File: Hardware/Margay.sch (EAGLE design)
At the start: 60 parts, among them IC1 ATMEGA644M, J1 CONN_4SCREW_2.54, J2 CONN_6, Q1 MOSFET_PCH-IRLML2244, Q2 MOSFET-NCH-DMG3404L, Q5 MOSFET_PCH-IRLML2244, U2 FT231X-Q

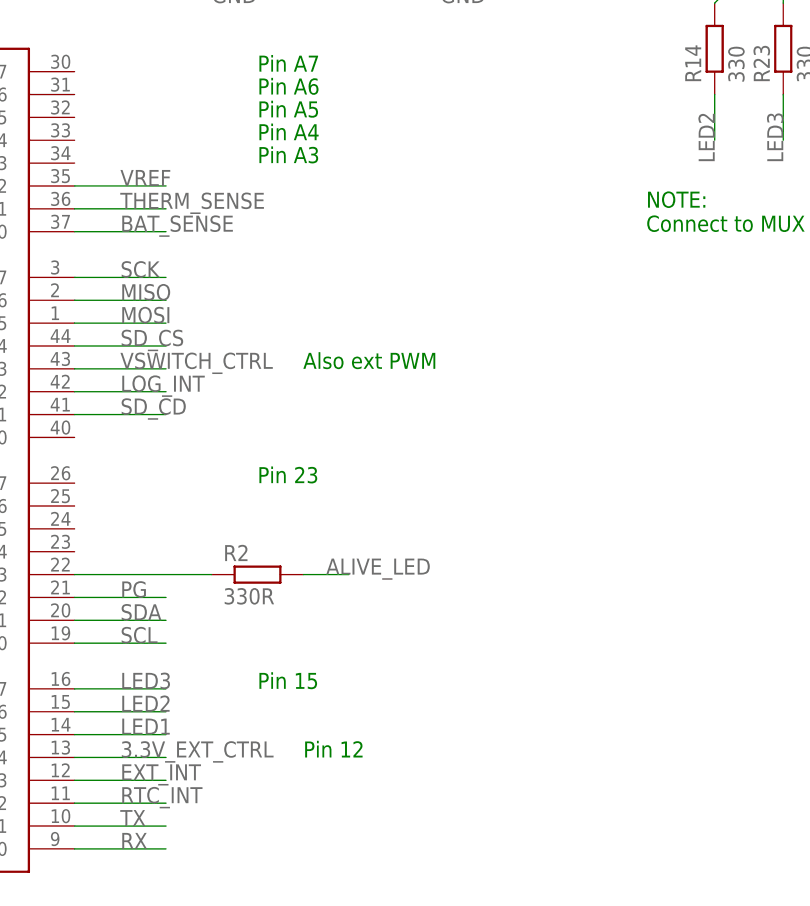
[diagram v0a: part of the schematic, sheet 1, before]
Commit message: Added software folder to repo
Software folder containing hardware test script as well as logger code which supports the TP-Downhole
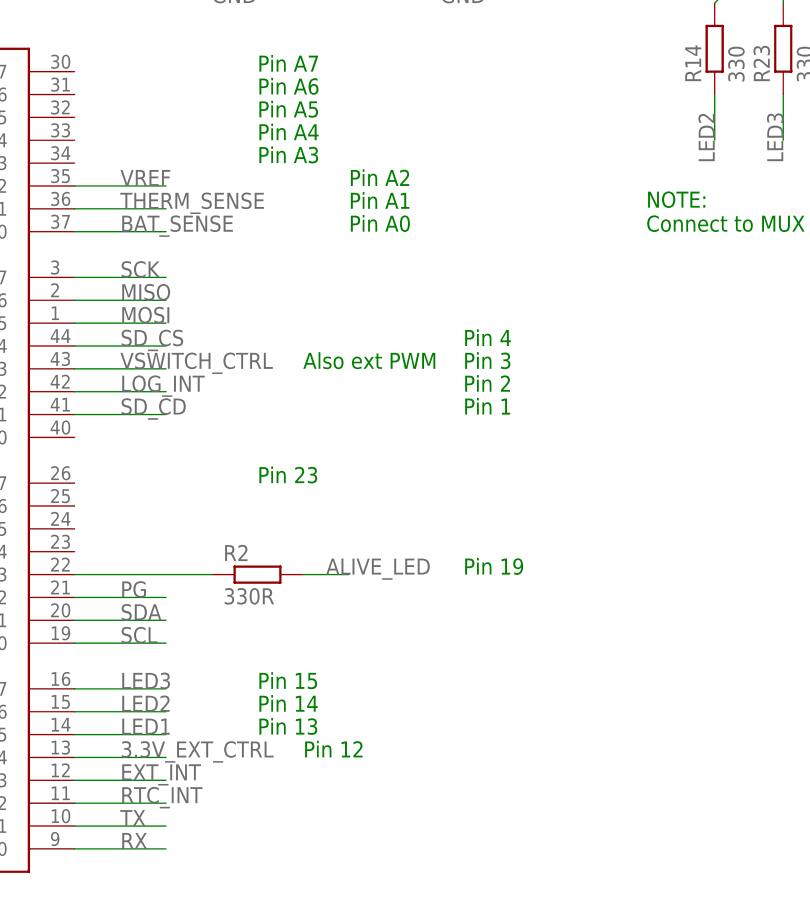
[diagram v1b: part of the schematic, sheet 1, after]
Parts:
- J2: value CONN_6 -> CONN_6SCREW_2.54; device bschulz:CONN_6 -> bschulz:CONN_6SCREW_2.54
- J3, J4, J5: device bschulz:CONN_022.54MM_SCREWTERM -> bschulz:CONN_02SCREW_2.54
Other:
- note added: "Pin 1"
- note added: "Pin 13"
- note added: "Pin 14"
- note added: "Pin 19"
- note added: "Pin 2"
- note added: "Pin 3"
- note added: "Pin 4"
- note added: "Pin A0"
- note added: "Pin A1"
- note added: "Pin A2"
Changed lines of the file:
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@@
 <layer number="18" name="Vias" color="2" fill="1" visible="no" active="no"/>
 <layer number="19" name="Unrouted" color="6" fill="1" visible="no" active="no"/>
-<layer number="20" name="Dimension" color="15" fill="1" visible="no" active="no"/>
+<layer number="20" name="Dimension" color="24" fill="1" visible="no" active="no"/>
 <layer number="21" name="tPlace" color="7" fill="1" visible="no" active="no"/>
 <layer number="22" name="bPlace" color="7" fill="1" visible="no" active="no"/>
@@
 <part name="GND32" library="supply1" library_urn="urn:adsk.eagle:library:371" deviceset="GND" device=""/>
 <part name="J1" library="bschulz" deviceset="CONN_4" device="SCREW_2.54"/>
-<part name="J2" library="bschulz" deviceset="CONN_6" device=""/>
-<part name="J3" library="bschulz" deviceset="CONN_02" device="2.54MM_SCREWTERM"/>
-<part name="J4" library="bschulz" deviceset="CONN_02" device="2.54MM_SCREWTERM"/>
-<part name="J5" library="bschulz" deviceset="CONN_02" device="2.54MM_SCREWTERM"/>
+<part name="J2" library="bschulz" deviceset="CONN_6" device="SCREW_2.54"/>
+<part name="J3" library="bschulz" deviceset="CONN_02" device="SCREW_2.54"/>
+<part name="J4" library="bschulz" deviceset="CONN_02" device="SCREW_2.54"/>
+<part name="J5" library="bschulz" deviceset="CONN_02" device="SCREW_2.54"/>
 <part name="R12" library="bschulz" deviceset="R-EU_" device="R0603" value="10k"/>
 <part name="JP2" library="SparkFun-Jumpers" library_urn="urn:adsk.eagle:library:528" deviceset="JUMPER-SMT_2_NC_PASTE" device="_SILK" package3d_urn="urn:adsk.eagle:package:39282/1"/>
@@
 <text x="327.66" y="231.14" size="1.778" layer="91">add voltage divider??</text>
 <text x="180.34" y="170.18" size="1.778" layer="91">Reverse Polarity Protection</text>
+<text x="175.26" y="55.88" size="1.778" layer="91">Pin 19</text>
+<text x="152.4" y="40.64" size="1.778" layer="91">Pin 14</text>
+<text x="152.4" y="38.1" size="1.778" layer="91">Pin 13</text>
+<text x="175.26" y="78.74" size="1.778" layer="91">Pin 3</text>
+<text x="175.26" y="76.2" size="1.778" layer="91">Pin 2</text>
+<text x="175.26" y="73.66" size="1.778" layer="91">Pin 1</text>
+<text x="175.26" y="81.28" size="1.778" layer="91">Pin 4</text>
+<text x="162.56" y="93.98" size="1.778" layer="91">Pin A0</text>
+<text x="162.56" y="96.52" size="1.778" layer="91">Pin A1</text>
+<text x="162.56" y="99.06" size="1.778" layer="91">Pin A2</text>
 </plain>
 <instances>

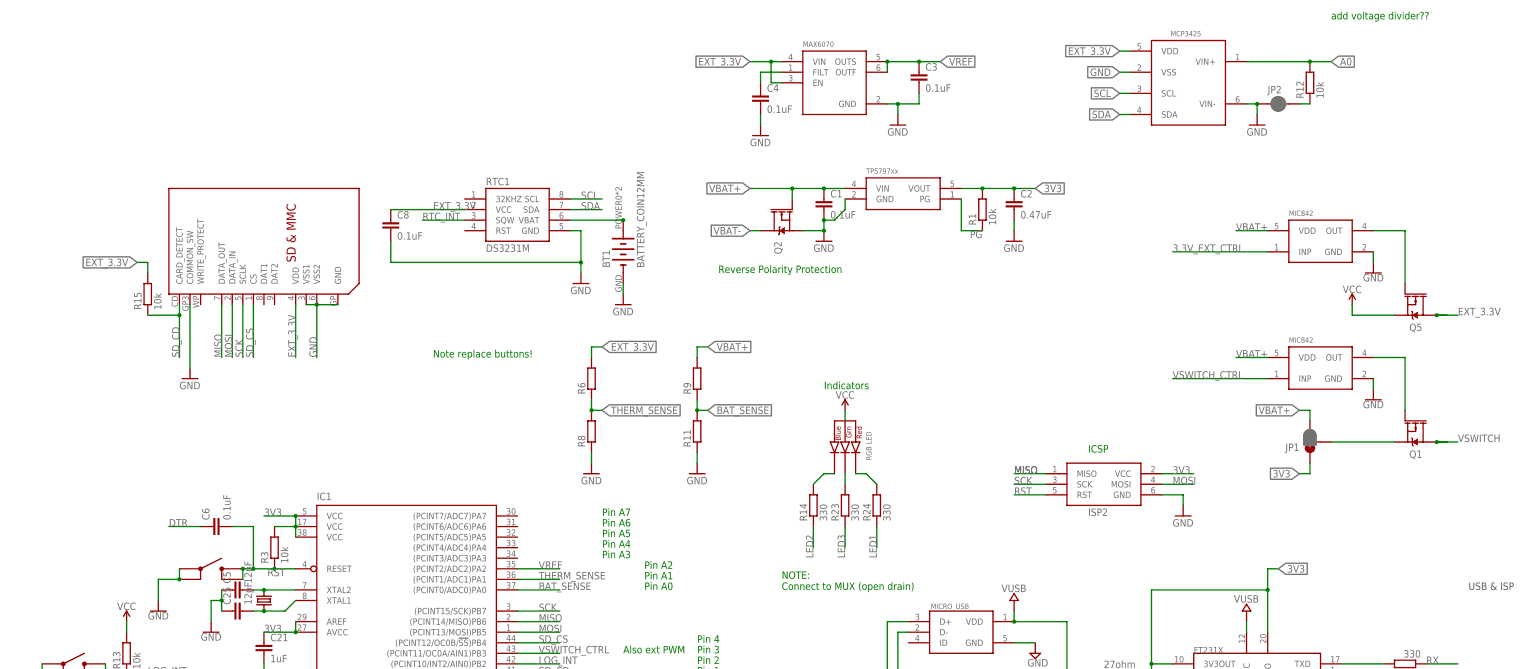
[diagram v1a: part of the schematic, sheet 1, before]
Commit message: Added revision notes to board
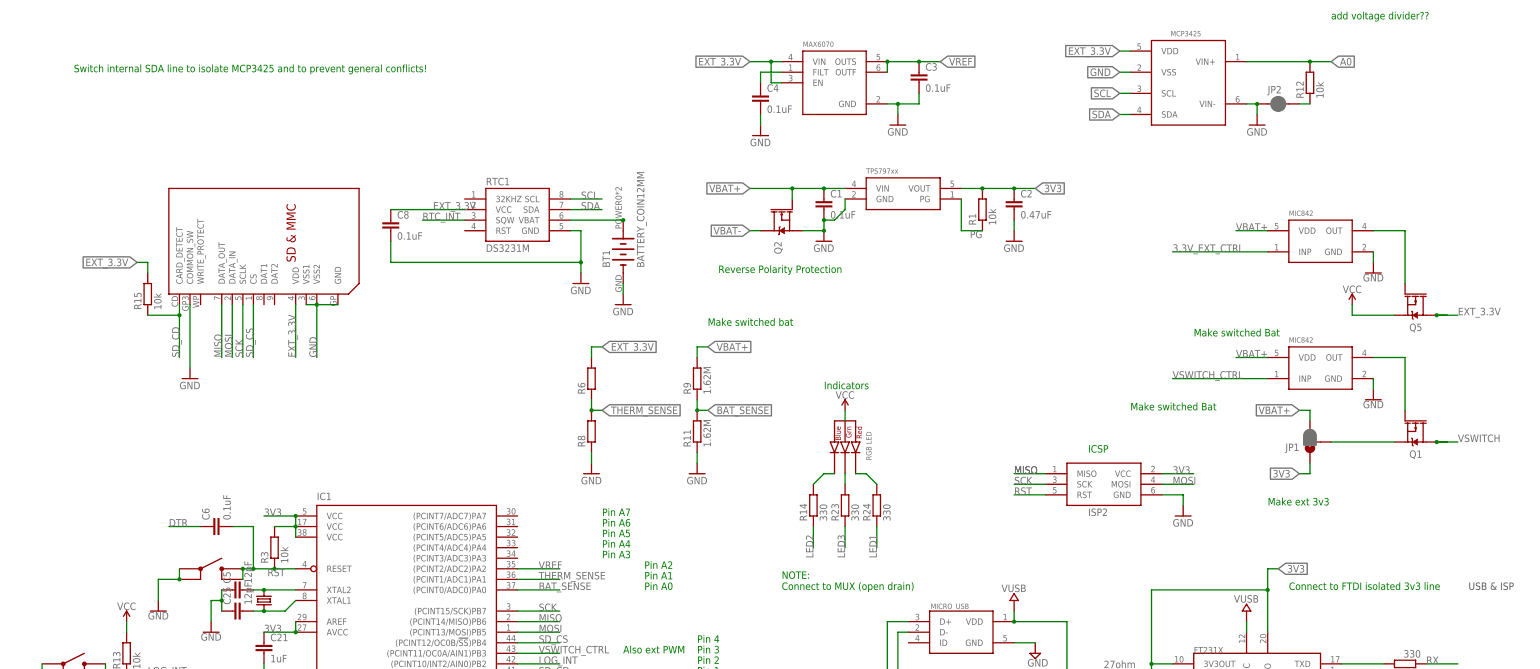
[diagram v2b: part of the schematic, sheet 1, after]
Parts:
- R11, R9: value (none) -> 1.62M
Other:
- note added: "Connect to FTDI isolated 3v3 line"
- note added: "Make ext 3v3"
- note added: "Make switched Bat"
- note added: "Make switched bat"
- note added: "Switch internal SDA line to isolate MCP3425 and to prevent general conflicts!"
- note removed: "Note replace buttons!"
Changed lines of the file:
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@@
 <part name="R6" library="bschulz" deviceset="R-EU_" device="R0603"/>
 <part name="R8" library="bschulz" deviceset="R-EU_" device="R0603"/>
-<part name="R9" library="bschulz" deviceset="R-EU_" device="R0603"/>
-<part name="R11" library="bschulz" deviceset="R-EU_" device="R0603"/>
+<part name="R9" library="bschulz" deviceset="R-EU_" device="R0603" value="1.62M"/>
+<part name="R11" library="bschulz" deviceset="R-EU_" device="R0603" value="1.62M"/>
 <part name="GND4" library="supply1" library_urn="urn:adsk.eagle:library:371" deviceset="GND" device=""/>
 <part name="GND5" library="supply1" library_urn="urn:adsk.eagle:library:371" deviceset="GND" device=""/>
@@
 <text x="195.58" y="93.98" size="1.778" layer="91">NOTE:
 Connect to MUX (open drain)</text>
-<text x="111.76" y="149.86" size="1.778" layer="91">Note replace buttons!</text>
 <text x="157.48" y="35.56" size="1.778" layer="91">Pin 12</text>
 <text x="152.4" y="111.76" size="1.778" layer="91">Pin A7</text>
@@
 <text x="162.56" y="96.52" size="1.778" layer="91">Pin A1</text>
 <text x="162.56" y="99.06" size="1.778" layer="91">Pin A2</text>
+<text x="312.42" y="114.3" size="1.778" layer="91">Make ext 3v3</text>
+<text x="279.4" y="137.16" size="1.778" layer="91">Make switched Bat</text>
+<text x="294.64" y="154.94" size="1.778" layer="91">Make switched Bat</text>
+<text x="177.8" y="157.48" size="1.778" layer="91">Make switched bat</text>
+<text x="25.4" y="218.44" size="1.778" layer="91">Switch internal SDA line to isolate MCP3425 and to prevent general conflicts!</text>
+<text x="317.5" y="93.98" size="1.778" layer="91">Connect to FTDI isolated 3v3 line</text>
 </plain>
 <instances>

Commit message: Margay 1.0 initial layout
Initial layout of the version 1.0 , solder jumpers currently not added, along with battery connector, may intoduce back later, needs cleanup and DRC
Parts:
- removed Q5: MOSFET_PCH-IRLML2244, bschulz:MOSFET_PCH-IRLML2244
- removed U$18: MIC842, bschulz:MIC842
- added C7: 0.1uF, bschulz_passives:C-EUC0603
- added C9: 0.47uF, bschulz_passives:C-EUC0603
- added Q3: 2N7002, bschulz:MOSFET-NCH-2N7002PW
- added Q4, Q6: FDN360P, bschulz:MOSFET_PCH-FDN360P
- added R16: 180k, bschulz_passives:R-EU_R0603
- added R17: 10k, bschulz_passives:R-EU_R0603
- added U$10: TPS79733, bschulz:TPS79733
- added U$11: MIC842H, bschulz:MIC842H
- added U$12, U$13: SN74LVC1G3157DRL, bschulz:SN74LVC1G3157DRL
- added U$17: SN74AUP3G34DCU, bschulz:SN74AUP3G34DCU
- D+, D-: device bschulz:R-EU_27R0603 -> bschulz_passives:R-EU_27R0603
- J1: value CONN_4SCREW_2.54 -> CONN_42.54_SCREW; device bschulz:CONN_4SCREW_2.54 -> bschulz:CONN_42.54_SCREW
- Q1: value MOSFET_PCH-IRLML2244 -> FDN360P; device bschulz:MOSFET_PCH-IRLML2244 -> bschulz:MOSFET_PCH-FDN360P
- Q2: value MOSFET-NCH-DMG3404L -> DMG3404
- R10, R4, R5, R7: device bschulz:R-EU_330R0603 -> bschulz_passives:R-EU_330R0603
- U$4: value MIC842 -> MIC842H; device bschulz:MIC842 -> bschulz:MIC842H
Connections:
- removed net 3.3V_EXT_CTRL: IC1.(PCINT28/OC1B)PD4, U$18.INP
- removed net EXT_3.3V: C8.1, J1.2, J2.2, Q5.D, R15.2, R6.2, RTC1.VCC, U$3.VDD, U$7.EN, U$7.VIN, U$8.VDD
- removed net N$7: Q5.G, U$18.OUT
- new net 3V3_AUX: C9.1, R15.2, R6.2, U$10.VOUT, U$12.A, U$12.VCC, U$13.VCC, U$17.VCC, U$3.VDD
- new net 3V3_AUX_CTRL: IC1.(PCINT28/OC1B)PD4, U$12.S, U$13.S
- new net 3V3_EXT: J1.3, J2.2, JP1.1, U$12.B2
- new net 3V3_FTDI: C14.1, Q4.D, U2.3V3OUT, U2.RESET#, U2.VCCIO
- new net 3V3_OB: C8.1, RTC1.VCC, U$12.B1, U$7.EN, U$7.VIN, U$8.VDD
- new net MOSI_BUF: J2.3, U$17.2Y, U$3.DATA_IN
- new net N$4: Q6.G, U$11.OUT
- new net N$6: Q3.D, Q4.G, R16.2
- new net SCK_BUF: J2.5, U$17.1Y, U$3.SCLK
- new net SDA_EXT: J1.2, U$13.B2
- new net SDA_OB: RTC1.SDA, U$13.B1, U$8.SDA
- new net SD_CS_BUF: U$17.3Y, U$3.CS
- new net VBAT_SW: C7.1, JP1.3, Q6.D, R9.2, U$10.VIN, U$4.VDD
- new net VBAT_SW_CTRL: IC1.(PCINT19/TMS)PC3, U$11.INP
- net 3V3: now also Q4.S, R16.1; no longer C14.1, JP1.1, Q5.S, U2.3V3OUT, U2.RESET#, U2.VCCIO
- net GND: now also C7.2, C9.2, J1.4, Q3.S, R17.1, U$10.GND, U$11.GND, U$12.GND, U$13.GND, U$17.GND; no longer J1.1, U$18.GND
- net MOSI: now also U$17.2A; no longer J2.3, U$3.DATA_IN
- net N$1: now also IC1.(PCINT20/TDO)PC4; no longer IC1.(PCINT19/TMS)PC3
- net SCK: now also U$17.1A; no longer J2.5, U$3.SCLK
- net SCL: now also J1.1; no longer J1.4
- net SDA: now also U$13.A; no longer J1.3, RTC1.SDA, U$8.SDA
- net SD_CS: now also U$17.3A; no longer U$3.CS
- net VBAT+: now also Q6.S, U$11.VDD; no longer JP1.3, R9.2, U$18.VDD, U$4.VDD
- net VUSB: now also Q3.G, R17.2
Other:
- note added: "Check polarity!"
- note added: "Jump SDA channels together, prevents using occupied addresses on the external I2C port"
- note added: "Jump auxillary power rails together, reduces brownout protection"
- note added: "Pin 20"
- note added: "Provide jumper for SDA switch and power switch"
- moved on the sheet: R2
